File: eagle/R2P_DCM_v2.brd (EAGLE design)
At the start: 40 x 60 mm, 53 parts, among them U1 STM32F103CX, U5 LD3985XX, X1 MICROMATCH-4, X2 OSC-XTAL212M_

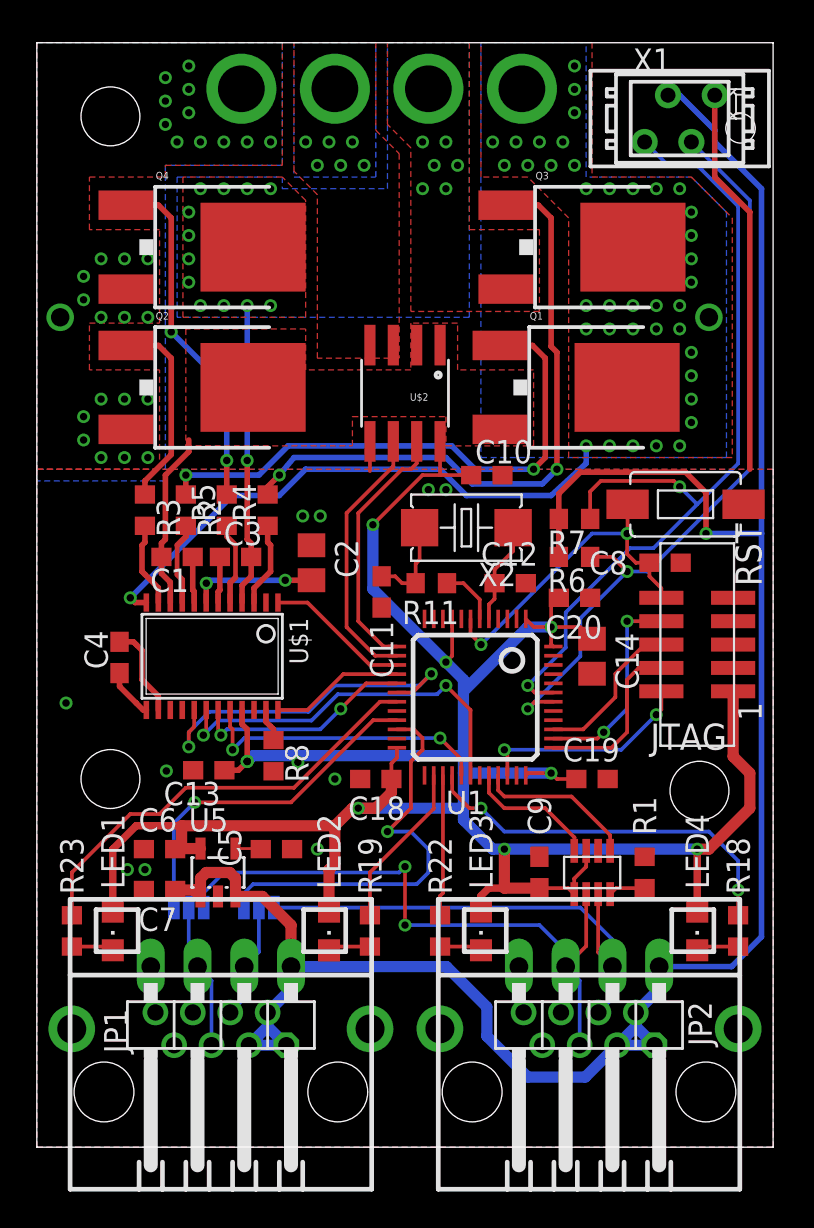
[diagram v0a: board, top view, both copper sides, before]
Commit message: Powerpad under A4940
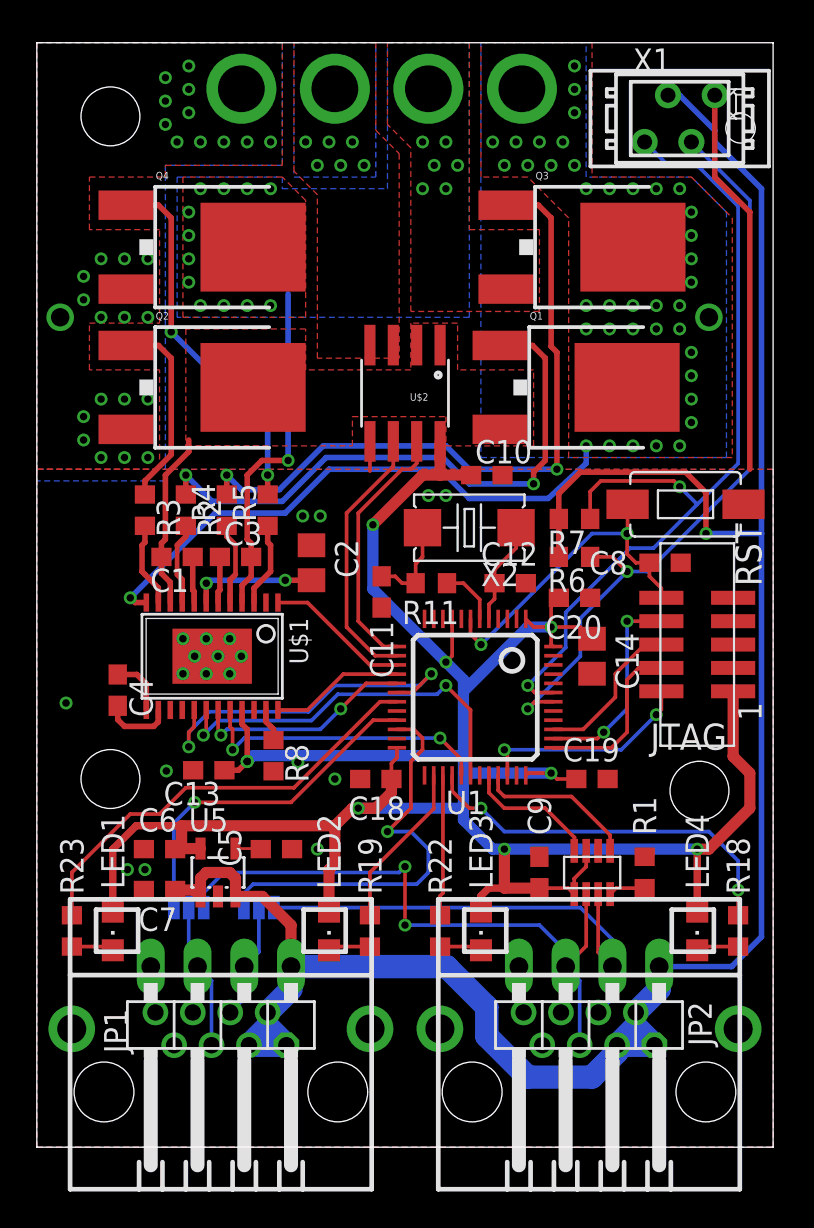
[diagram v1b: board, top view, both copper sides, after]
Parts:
- moved R4 2.22 mm to (10.3, 34.6)
- moved R5 2.22 mm to (12.5, 34.6)
- moved C4 1.78 mm to (4.40, 24.8), turned to 270 degrees
- moved X2 0.16 mm to (23.5, 33.7)
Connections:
- net GND: now also U$1.PAD
- net HVG2: now also U$1.5; no longer U$1.3
- net LVG2: now also U$1.3; no longer U$1.5
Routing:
- net N$7: track 34.3 -> 37.4 mm
- net VM2: track 16.4 -> 18.8 mm
- net N$5: track 30.2 -> 31.9 mm
- net N$11: track 5.02 -> 3.85 mm
- net N$9: track 19.0 -> 19.9 mm
- net GND: vias 40 -> 49
